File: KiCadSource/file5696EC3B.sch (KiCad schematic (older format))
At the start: 49 parts, among them J1 DIL14_RA, U15 74AVCH16T245

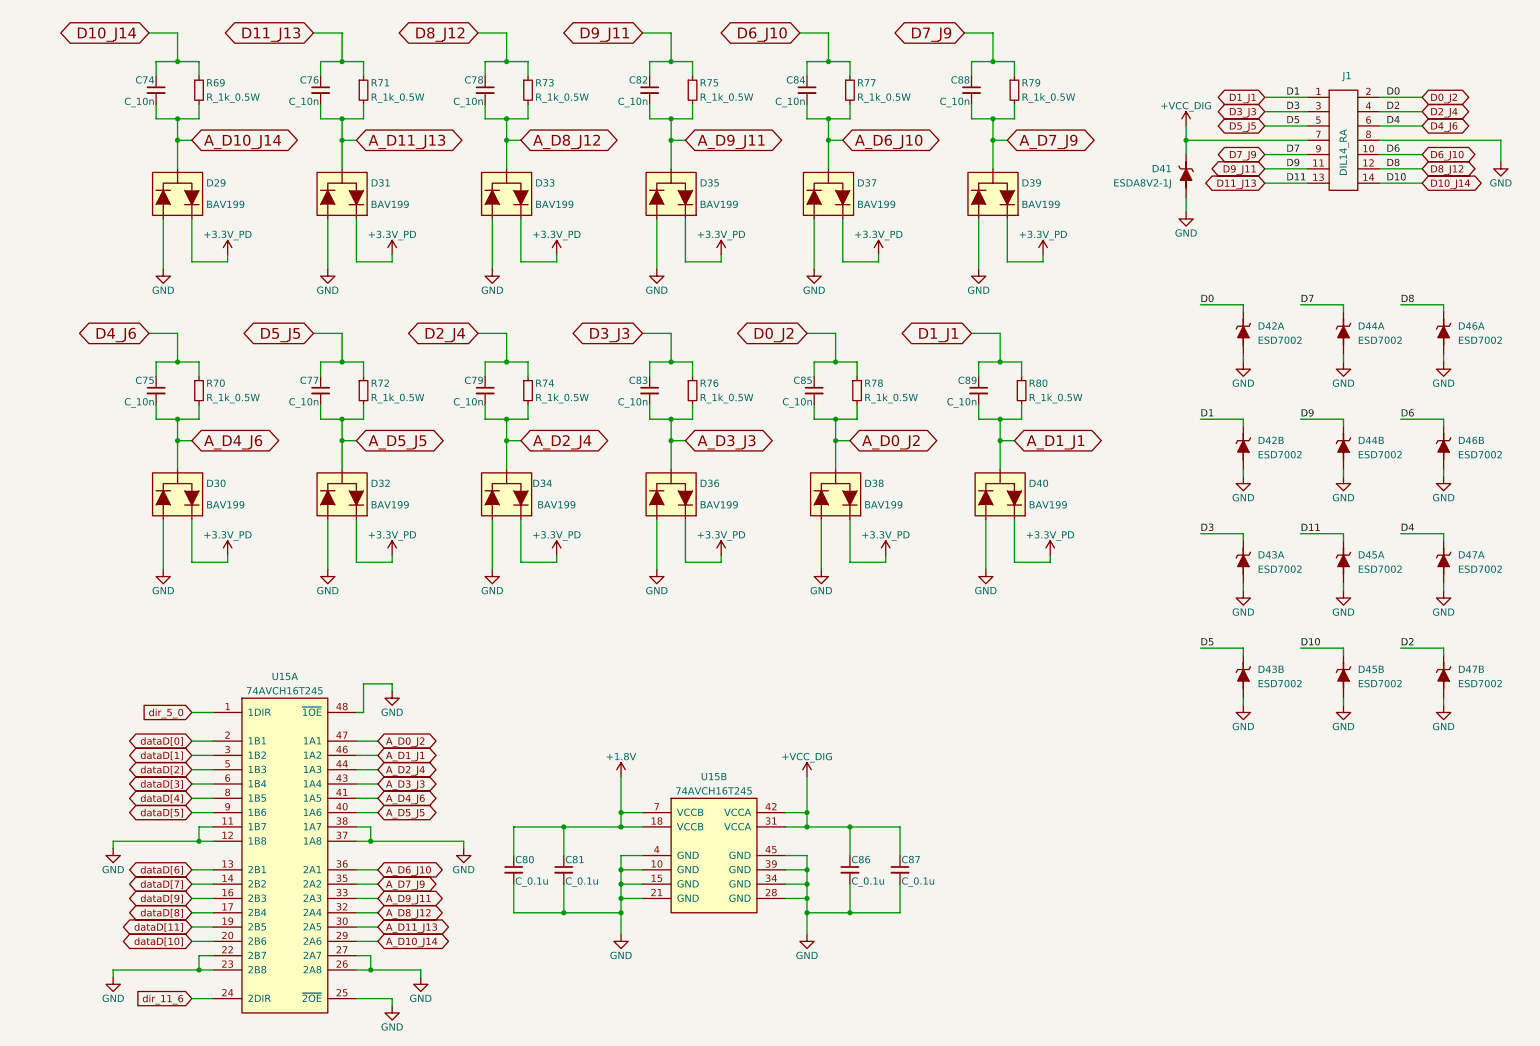
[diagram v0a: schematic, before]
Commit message: first production run, digital GPIOs, replaced parts (see CHANGES.txt)
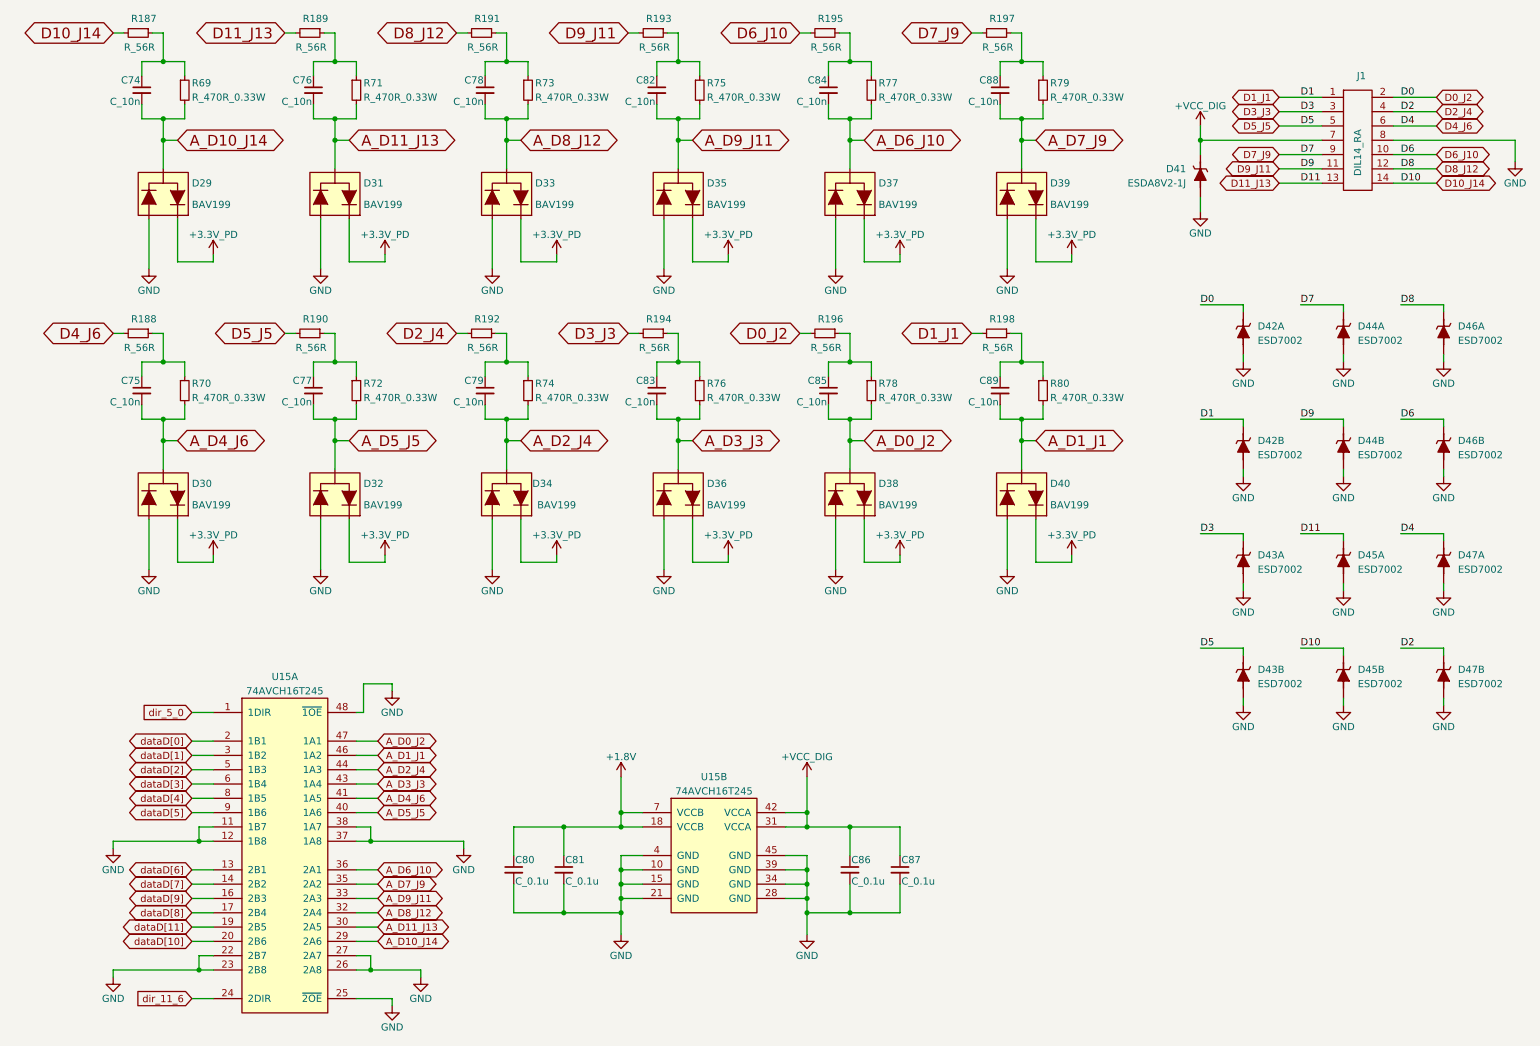
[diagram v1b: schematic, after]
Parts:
- removed R69, R70, R71, R72, R73, R74, R75, R76, R77, R78, R79, R80: R_1k_0.5W, ScopefunPackagesLibrary:R_0805, symbol R_1k_0.5W
- added R187, R188, R189, R190, R191, R192, R193, R194, R195, R196, R197, R198: R_56R, ScopefunPackagesLibrary:R_0603, symbol R_56R
- added R69, R70, R71, R72, R73, R74, R75, R76, R77, R78, R79, R80: R_470R_0.33W, ScopefunPackagesLibrary:R_0603, symbol R_470R_0.33W
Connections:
- net A_D0_J2: now also R78.2
- net A_D10_J14: now also R69.2
- net A_D11_J13: now also R71.2
- net A_D1_J1: now also R80.2
- net A_D2_J4: now also R74.2
- net A_D3_J3: now also R76.2
- net A_D4_J6: now also R70.2
- net A_D5_J5: now also R72.2
- net A_D6_J10: now also R77.2
- net A_D7_J9: now also R79.2
- net A_D8_J12: now also R73.2
- net A_D9_J11: now also R75.2
- net D0_J2: now also R196.2; no longer C85.1
- net D10_J14: now also R187.2; no longer C74.1
- net D11_J13: now also R189.2; no longer C76.1
- net D1_J1: now also R198.2; no longer C89.1
- net D2_J4: now also R192.2; no longer C79.1
- net D3_J3: now also R194.2; no longer C83.1
- net D4_J6: now also R188.2; no longer C75.1
- net D5_J5: now also R190.2; no longer C77.1
- net D6_J10: now also R195.2; no longer C84.1
- net D7_J9: now also R197.2; no longer C88.1
- net D8_J12: now also R191.2; no longer C78.1
- net D9_J11: now also R193.2; no longer C82.1
- new net: C74.1, R187.1, R69.1
- new net: C76.1, R189.1, R71.1
- new net: C78.1, R191.1, R73.1
- new net: C82.1, R193.1, R75.1
- new net: C84.1, R195.1, R77.1
- new net: C88.1, R197.1, R79.1
- new net: C75.1, R188.1, R70.1
- new net: C77.1, R190.1, R72.1
- new net: C79.1, R192.1, R74.1
- new net: C83.1, R194.1, R76.1
- new net: C85.1, R196.1, R78.1
- new net: C89.1, R198.1, R80.1
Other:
- moved on the sheet: C74, C75, C76, C77, C82, C83, C84, C85, C88, C89, D29, D30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
